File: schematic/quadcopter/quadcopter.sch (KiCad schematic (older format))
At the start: 22 parts, among them SW1 SW_SPST, U1 MATEK_PDB-XT60, U10 iFlight_XING_E_2207, U11 iFlight_XING_E_2207, U12 iFlight_XING_E_2207, U13 iFlight_XING_E_2207, U14 ST-LINK, U2 nRF24L01+PA+LNA_BreakOut, U3 LM358N, U4 WEACT_STM32F411CEU6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

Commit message: Update quadcopter schematic
- redrawing for readability
- add rf transceiver module
- remove opamp used for battery monitoring
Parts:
- removed BZ1: Buzzer, symbol Device:Buzzer
- removed D1, D2: LED, symbol Device:LED
- removed R1: 470K, symbol Device:R
- removed R2: 100K, symbol Device:R
- removed R3, R4: 330K, symbol Device:R
- removed SW1: SW_SPST, symbol Switch:SW_SPST
- removed U1: MATEK_PDB-XT60, symbol quadcopter-rescue:MATEK_PDB-XT60-quadcopter_symbol
- removed U10, U11, U12, U13: iFlight_XING_E_2207, symbol quadcopter-rescue:iFlight_XING_E_2207-quadcopter_symbol
- removed U14: ST-LINK, symbol quadcopter-rescue:ST-LINK
- removed U2: nRF24L01+PA+LNA_BreakOut, symbol quadcopter-rescue:nRF24L01+PA+LNA_BreakOut-quadcopter_symbol
- removed U3: LM358N, symbol quadcopter-rescue:LM358N-quadcopter_symbol
- removed U4: WEACT_STM32F411CEU6, symbol quadcopter-rescue:WEACT_STM32F411CEU6-quadcopter_symbol
- removed U5, U7, U8, U9: HAKRC_35A_ESC, symbol quadcopter-rescue:HAKRC_35A_ESC-quadcopter_symbol
- removed U6: ICM_20948_BreakOut, symbol quadcopter-rescue:ICM_20948_BreakOut-quadcopter_symbol
- added R?: 470k, symbol Device:R_US
- added R?: 100k, symbol Device:R_US
- added U?: WeAct_Black_Pill_V3.0(STM32F411CEU6), symbol quadcopter-rescue:WeAct_Black_Pill_V3.0(STM32F411CEU6)
- added U?: SparkFun_9Dof_IMU_Breakout-ICM-20948(Qwiic), symbol quadcopter-rescue:SparkFun_9Dof_IMU_Breakout-ICM-20948(Qwiic)
- added U?: ST-LINK, symbol quadcopter-rescue:ST-LINK
- added U?: nrf24l01+pa+lna_rf_transceiver_module, symbol quadcopter-rescue:nrf24l01+pa+lna_rf_transceiver_module
- added U?: Matek_PDB-XT60_3-4S, symbol quadcopter-rescue:Matek_PDB-XT60_3-4S
- added U?: 4S_Lipo_Battery, symbol quadcopter-rescue:4S_Lipo_Battery
- added U? (x4): HAKRC_BLHeli_32Bit_35A_2-5S_ESC, symbol quadcopter-rescue:HAKRC_BLHeli_32Bit_35A_2-5S_ESC
- added U? (x4): iFlight_XING-E_2207_2450KV, symbol quadcopter-rescue:iFlight_XING-E_2207_2450KV
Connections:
- net labels added: +3.3V, +5V, ADC_IN, CE, SPI1_CS, SPI1_MISO, SPI1_MOSI, SPI1_SCLK, SPI2_CSN, SPI2_MISO, SPI2_MOSI, SPI2_SCK, SWCLK, SWDIO, TIM2_CH1, TIM2_CH3, TIM5_CH2, TIM5_CH4
- net labels removed: +BATT
- wire segments 131 -> 97
- no-connect marks 0 -> 15
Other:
- note added: "ESC & MOTOR"
- note added: "IMU (ICM20948)"
- note added: "MCU Module"
- note added: "Motor 1"
- note added: "Motor 2"
- note added: "Motor 3"
- note added: "Motor 4"
- note added: "PDB"
- note added: "RF transceiver (nrf24l01)"

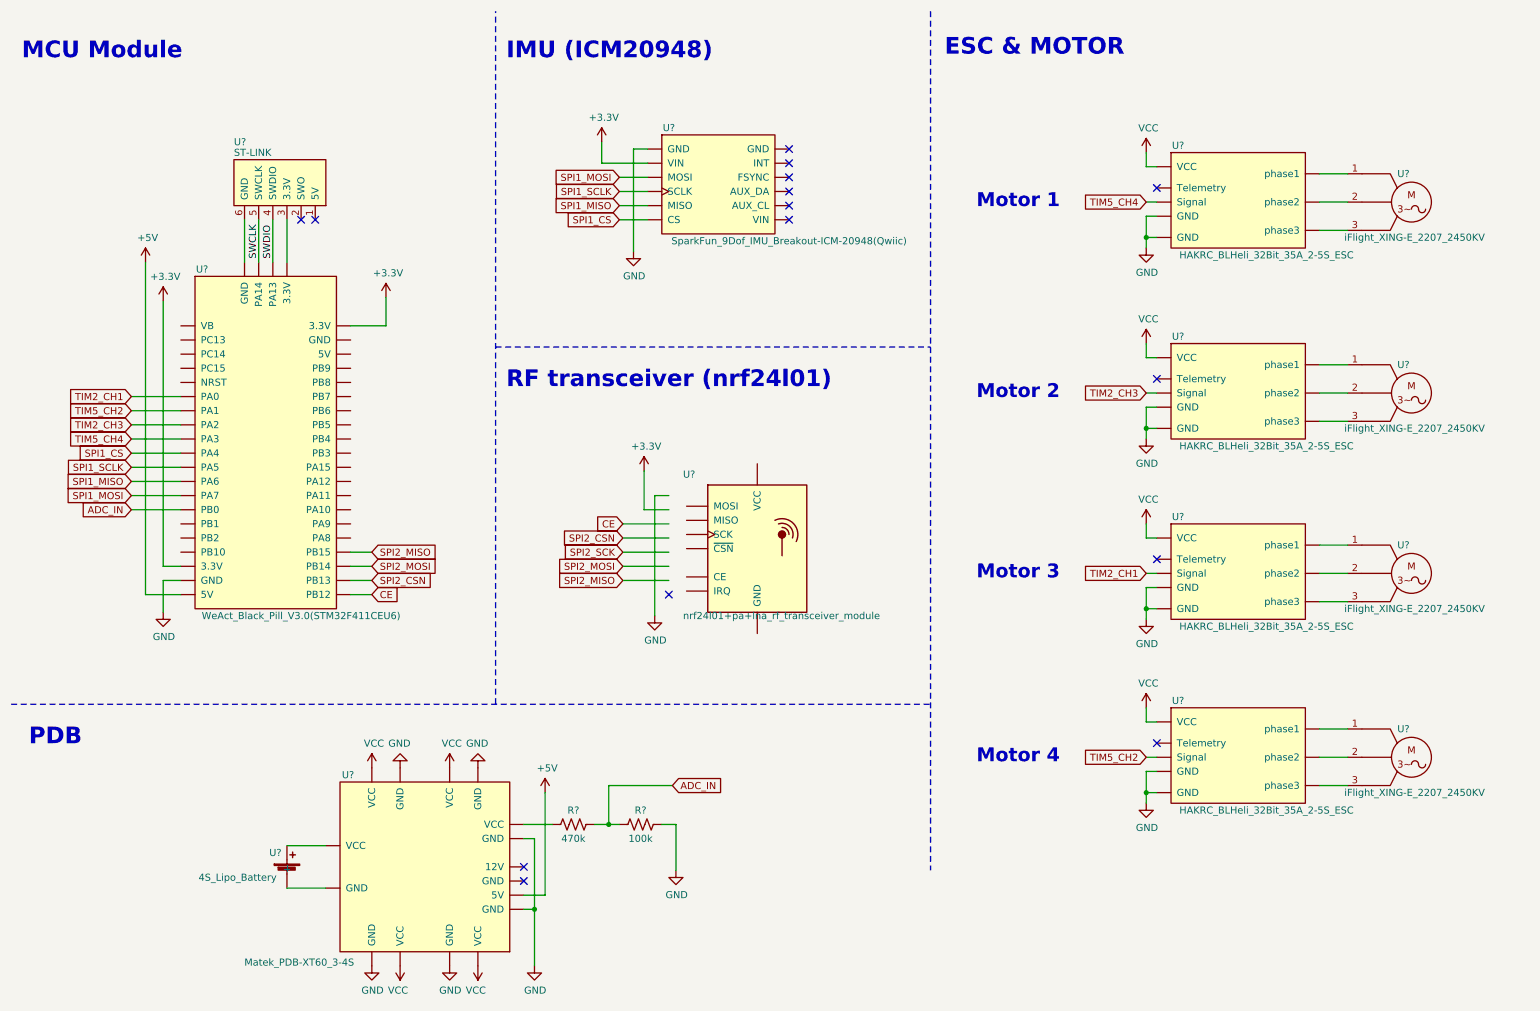
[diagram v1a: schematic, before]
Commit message: Add controller schematic
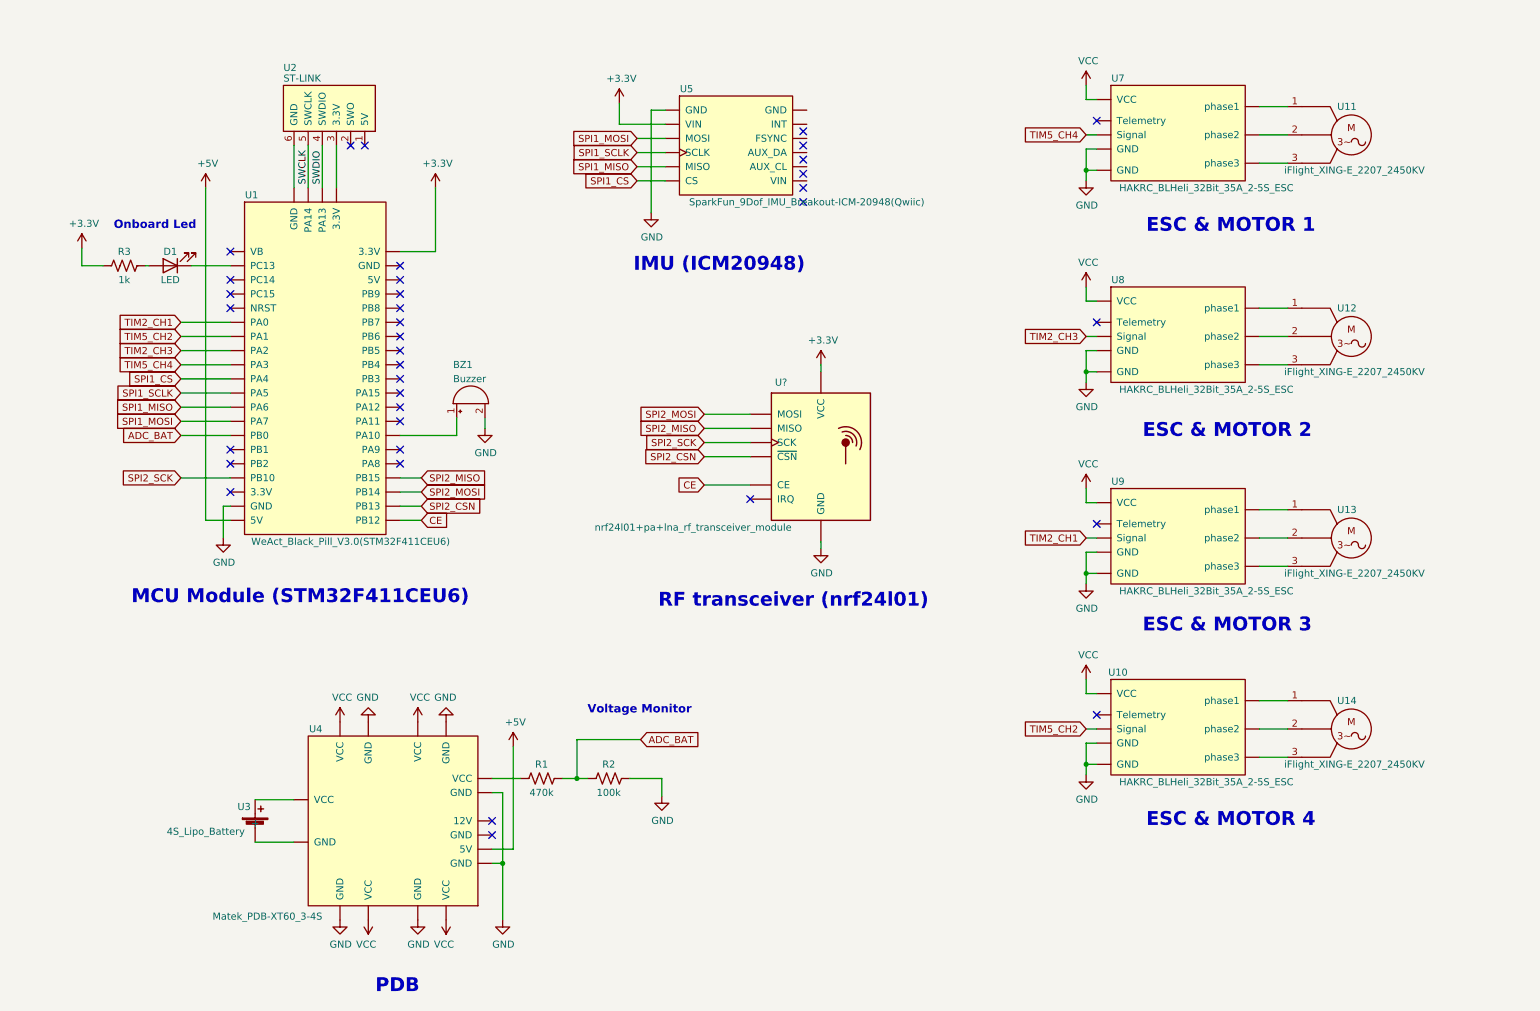
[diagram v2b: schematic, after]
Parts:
- removed U?: nrf24l01+pa+lna_rf_transceiver_module, symbol quadcopter-rescue:nrf24l01+pa+lna_rf_transceiver_module
- added BZ1: Buzzer, symbol Device:Buzzer
- added D1: LED, symbol Device:LED
- added R3: 1k, symbol Device:R_US
- added U?: nrf24l01+pa+lna_rf_transceiver_module, symbol quadcopter-rescue:nrf24l01+pa+lna_rf_transceiver_module
- gave numbers to parts that had none: 15
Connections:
- net labels added: ADC_BAT
- net labels removed: ADC_IN
- wire segments 97 -> 101
- no-connect marks 15 -> 36
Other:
- note added: "ESC & MOTOR 1"
- note added: "ESC & MOTOR 2"
- note added: "ESC & MOTOR 3"
- note added: "ESC & MOTOR 4"
- note added: "MCU Module (STM32F411CEU6)"
- note added: "Onboard Led"
- note added: "Voltage Monitor"
- note removed: "ESC & MOTOR"
- note removed: "MCU Module"
- note removed: "Motor 1"
- note removed: "Motor 2"
- note removed: "Motor 3"
- note removed: "Motor 4"
- moved on the sheet: R1, R2, U1, U10, U11, U12, U13, U14, U2, U3, U4, U5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
